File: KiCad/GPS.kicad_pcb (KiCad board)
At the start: 2 copper layers, 36 x 24.5 mm, 36 parts, among them J1 DC, J2 I/O, J3 USB-C, U1 ESP32-PICO-MINI-02, U2 L96-M33, U3 FT231XQ, U4 LMR16006+FB, U5 QR

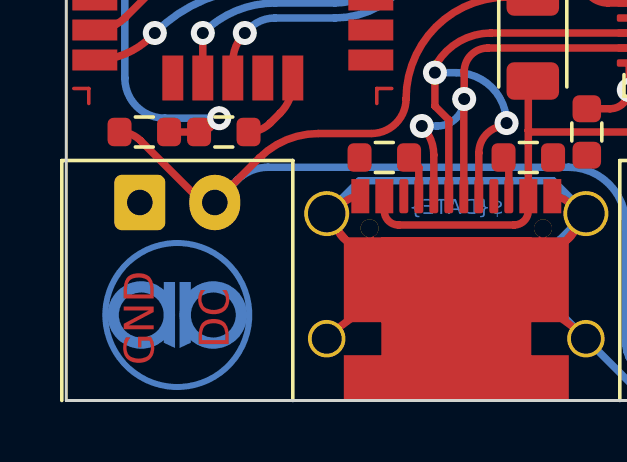
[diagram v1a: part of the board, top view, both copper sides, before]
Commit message: Updated for VBUS and GPIO changes
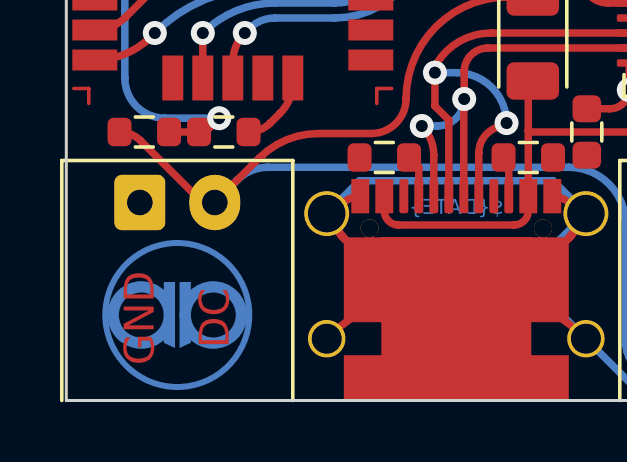
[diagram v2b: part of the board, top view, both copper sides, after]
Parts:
- R6: value 500K -> 470K
- moved Logo1 2.40 mm to (87.8, 139.4)

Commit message: Tidy
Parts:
- U3: footprint Package_DFN_QFN:QFN-20-1EP_4x4mm_P0.5mm_EP2.5x2.5mm -> RevK:QFN-20-1EP_4x4mm_P0.5mm_EP2.5x2.5mm
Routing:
- net GND: track 118.8 -> 114.9 mm
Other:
- board text removed: "${DATE}"

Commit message: Tidy
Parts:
- moved Logo2 0.43 mm to (115.7, 122.9)
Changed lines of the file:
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@@
   )
   (footprint "RevK:AJK" (layer "B.Cu")
-    (at 115.7 123.3 180)
+    (at 115.65 122.875 180)
     (property "Note" "Non part, PCB printed")
     (property "Sheetfile" "GPS.kicad_sch")
@@
       (effects (font (size 1 1) (thickness 0.15)) (justify mirror))
     )
+    (fp_text user "www.me.uk" (at -0.58 -3.75 unlocked) (layer "B.SilkS")
+      (effects (font (size 0.65 0.65) (thickness 0.1)) (justify mirror))
+    )
     (fp_line (start 0 0) (end 1.8 -2.1) (layer "B.Cu") (width 0.25))
-    (fp_line (start -0.85 -2.11) (end -0.75 -2.11) (layer "B.Cu") (width 0.08))
-    (fp_line (start 0 2.1) (end -3 -2.1) (layer "B.Cu") (width 0.25))
-    (fp_line (start 1.8 2) (end 0 0) (layer "B.Cu") (width 0.25))
     (fp_line (start 0 2.1) (end 0 -2.1) (layer "B.Cu") (width 0.25))
     (fp_line (start -0.85 -1.95) (end -0.75 -1.95) (layer "B.Cu") (width 0.08))
+    (fp_line (start 1.8 2) (end 0 0) (layer "B.Cu") (width 0.25))
     (fp_line (start -0.75 -2.11) (end -0.65 -2.25) (layer "B.Cu") (width 0.08))
+    (fp_line (start 0 2.1) (end -3 -2.1) (layer "B.Cu") (width 0.25))
+    (fp_line (start -0.85 -2.11) (end -0.75 -2.11) (layer "B.Cu") (width 0.08))
     (fp_line (start -0.85 -1.95) (end -0.85 -2.25) (layer "B.Cu") (width 0.08))
     (fp_line (start 0 0) (end -1.5 0) (layer "B.Cu") (width 0.25))
+    (fp_arc (start -1.5 -2.1) (mid -0.75 -2.85) (end 0 -2.1) (layer "B.Cu") (width 0.25))
     (fp_arc (start -0.75 -2.11) (mid -0.67 -2.03) (end -0.75 -1.95) (layer "B.Cu") (width 0.08))
-    (fp_arc (start -1.5 -2.1) (mid -0.75 -2.85) (end 0 -2.1) (layer "B.Cu") (width 0.25))
     (fp_circle (center -0.77 -2.11) (end -0.47 -2.11) (layer "B.Cu") (width 0.08) (fill none))
-    (fp_line (start 0 0) (end -1.5 0) (layer "B.Mask") (width 0.45))
+    (fp_line (start 0 2.1) (end 0 -2.1) (layer "B.Mask") (width 0.45))
     (fp_line (start 1.8 2) (end 0 0) (layer "B.Mask") (width 0.45))
     (fp_line (start 0 2.1) (end -3 -2.1) (layer "B.Mask") (width 0.45))
-    (fp_line (start 0 2.1) (end 0 -2.1) (layer "B.Mask") (width 0.45))
+    (fp_line (start 0 0) (end -1.5 0) (layer "B.Mask") (width 0.45))
     (fp_line (start 0 0) (end 1.8 -2.1) (layer "B.Mask") (width 0.45))
     (fp_arc (start -1.5 -2.1) (mid -0.75 -2.85) (end 0 -2.1) (layer "B.Mask") (width 0.45))

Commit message: Fix BOM
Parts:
- R11: value 324R -> 220R
- R9: value 732R -> 680R
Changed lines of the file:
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@@
       (effects (font (size 0.5 0.5) (thickness 0.08)))
     )
-    (fp_text value "732R" (at 0 0 90) (layer "F.Fab")
+    (fp_text value "680R" (at 0 0 90) (layer "F.Fab")
       (effects (font (size 0.4 0.4) (thickness 0.08)))
     )
@@
       (effects (font (size 0.5 0.5) (thickness 0.08)))
     )
-    (fp_text value "324R" (at 0 0 90) (layer "F.Fab")
+    (fp_text value "220R" (at 0 0 90) (layer "F.Fab")
       (effects (font (size 0.4 0.4) (thickness 0.08)))
     )
@@
     (property "Sheetfile" "GPS.kicad_sch")
     (property "Sheetname" "")
-    (attr through_hole)
+    (property "exclude_from_bom" "")
+    (attr through_hole exclude_from_bom)
     (fp_text reference "Logo1" (at 0 -2.75) (layer "B.SilkS") hide
       (effects (font (size 1 1) (thickness 0.15)) (justify mirror))
@@
     (property "Sheetfile" "GPS.kicad_sch")
     (property "Sheetname" "")
-    (attr exclude_from_pos_files)
+    (property "exclude_from_bom" "")
+    (attr exclude_from_pos_files exclude_from_bom)
     (fp_text reference "JP6" (at 0 1.8 90) (layer "B.SilkS") hide
       (effects (font (size 1 1) (thickness 0.15)) (justify mirror))
@@
     (property "Sheetfile" "GPS.kicad_sch")
     (property "Sheetname" "")
-    (attr exclude_from_pos_files)
+    (property "exclude_from_bom" "")
+    (attr exclude_from_pos_files exclude_from_bom)
     (fp_text reference "JP4" (at 0 1.8 90) (layer "B.SilkS") hide
       (effects (font (size 1 1) (thickness 0.15)) (justify mirror))
@@
     (property "Sheetfile" "GPS.kicad_sch")
     (property "Sheetname" "")
-    (attr exclude_from_pos_files)
+    (property "exclude_from_bom" "")
+    (attr exclude_from_pos_files exclude_from_bom)
     (fp_text reference "JP3" (at 0 1.8 90) (layer "B.SilkS") hide
       (effects (font (size 1 1) (thickness 0.15)) (justify mirror))
@@
     (property "Sheetfile" "GPS.kicad_sch")
     (property "Sheetname" "")
-    (attr exclude_from_pos_files)
+    (property "exclude_from_bom" "")
+    (attr exclude_from_pos_files exclude_from_bom)
     (fp_text reference "JP2" (at 0 1.8 90) (layer "B.SilkS") hide
       (effects (font (size 1 1) (thickness 0.15)) (justify mirror))
@@
     (property "Sheetfile" "GPS.kicad_sch")
     (property "Sheetname" "")
-    (attr exclude_from_pos_files)
+    (property "exclude_from_bom" "")
+    (attr exclude_from_pos_files exclude_from_bom)
     (fp_text reference "JP1" (at 0 1.8 90) (layer "B.SilkS") hide
       (effects (font (size 1 1) (thickness 0.15)) (justify mirror))
@@
     (property "Sheetfile" "GPS.kicad_sch")
     (property "Sheetname" "")
-    (attr exclude_from_pos_files)
+    (property "exclude_from_bom" "")
+    (attr exclude_from_pos_files exclude_from_bom)
     (fp_text reference "JP5" (at 0 1.8 90) (layer "B.SilkS") hide
       (effects (font (size 1 1) (thickness 0.15)) (justify mirror))

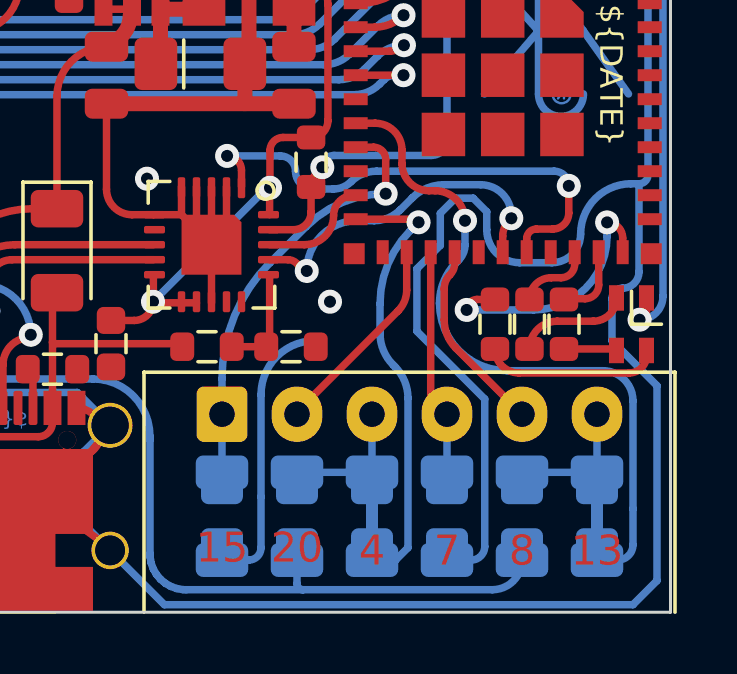
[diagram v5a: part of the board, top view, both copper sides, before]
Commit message: Swapped two pins over concerns that GPIO20 may be limited usage
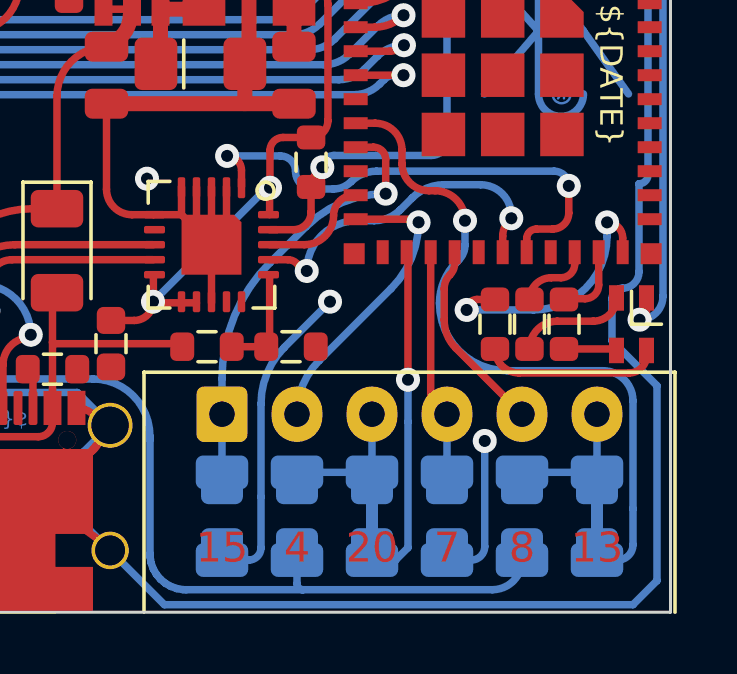
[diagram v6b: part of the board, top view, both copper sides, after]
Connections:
- U1 pad 24: IO3 -> IO2
- U1 pad 26: IO2 -> IO3
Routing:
- net GND: track 114.9 -> 97.6 mm, vias 6 -> 7
- net IO3: track 15.0 -> 11.2 mm
- net IO2: track 6.87 -> 9.94 mm, vias 0 -> 1

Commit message: Silkscreen tidy
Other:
- board text added: "34: BATADC 14: GPSTICK 33: GPSRST 27: GPSON 25: GPSTX 26: GPSRX"
- board text removed: "34: BAT 14: TICK 33: RST 27: ON 25: TX 26: RX"
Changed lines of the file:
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@@
     (effects (font (size 0.75 0.75) (thickness 0.1)) (justify mirror))
   )
-  (gr_text "34: BAT\n14: TICK\n33: RST\n27: ON\n25: TX\n26: RX" (at 93.3 126) (layer "B.SilkS")
+  (gr_text "34: BATADC\n14: GPSTICK\n33: GPSRST\n27: GPSON\n25: GPSTX\n26: GPSRX" (at 93.3 126) (layer "B.SilkS")
     (effects (font (size 0.75 0.75) (thickness 0.1)) (justify left mirror))
   )
